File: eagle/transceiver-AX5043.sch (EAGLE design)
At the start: 43 parts, among them J1 142-0701-851, J2 142-0701-851, J3 142-0701-851, U1 U-ONSEMI-AX5043, U2 LP2985XX-N, X1 TAITIEN-TY

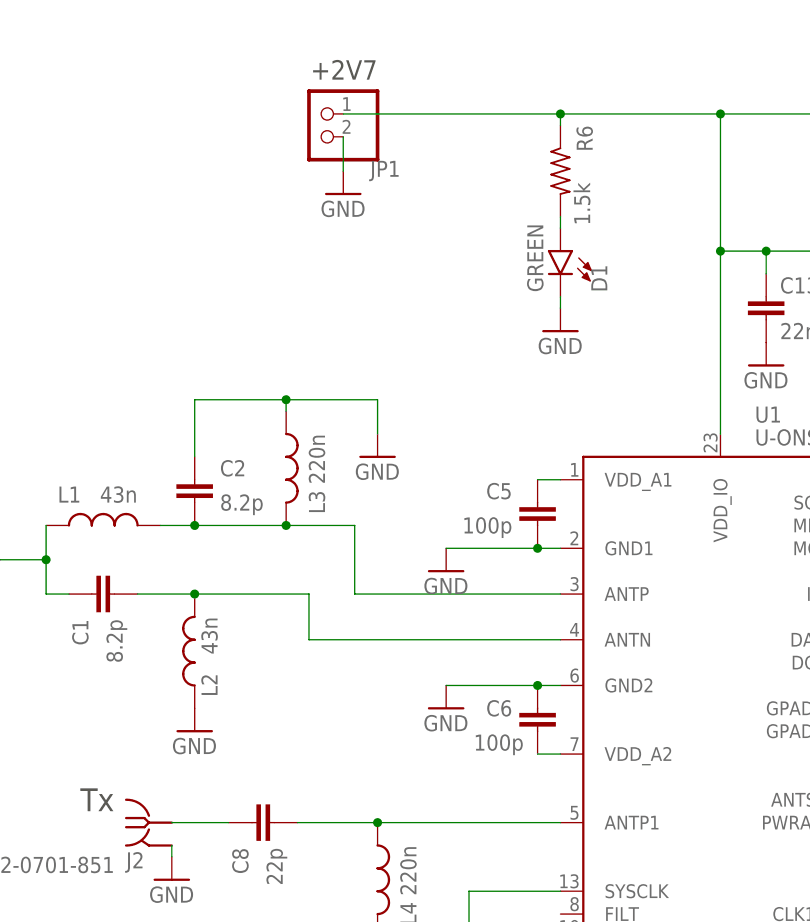
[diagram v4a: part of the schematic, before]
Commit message: Update AX5043
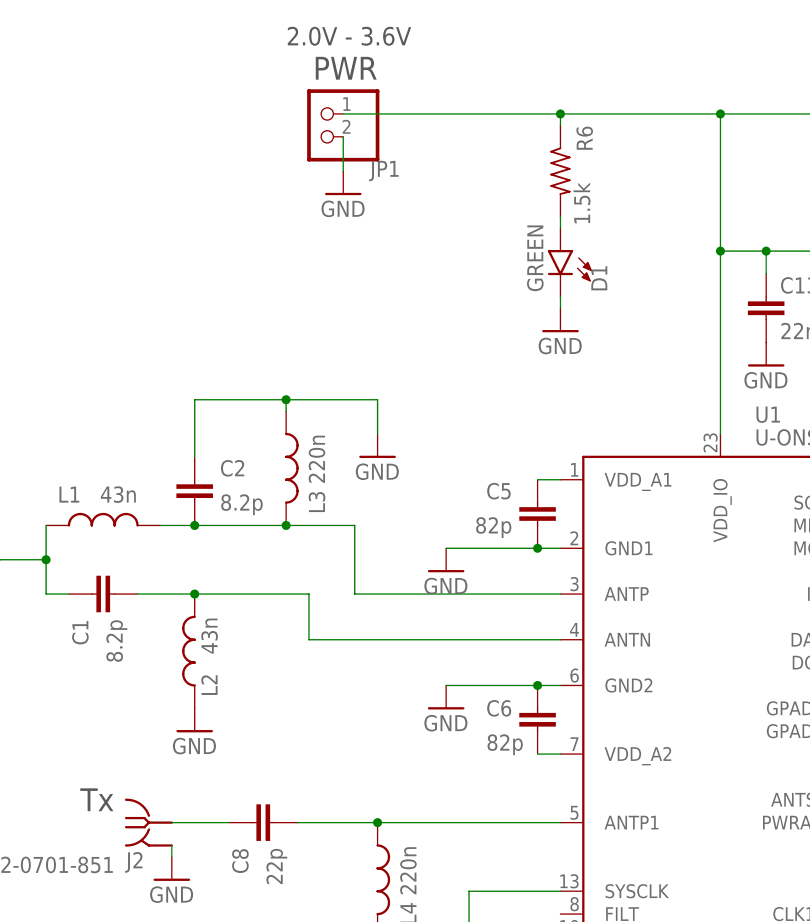
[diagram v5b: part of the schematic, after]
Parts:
- C5, C6: value 100p -> 82p
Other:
- note added: "2.0V - 3.6V"
- note added: "PWR"
- note removed: "+2V7"
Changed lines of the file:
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@@
 <?xml version="1.0" encoding="utf-8"?>
 <!DOCTYPE eagle SYSTEM "eagle.dtd">
-<eagle version="9.2.2">
+<eagle version="9.5.1">
 <drawing>
 <settings>
@@
 <part name="X1" library="X-Taitien-TY-TCXO" deviceset="TAITIEN-TY" device=""/>
 <part name="GND13" library="supply1" library_urn="urn:adsk.eagle:library:371" deviceset="GND" device=""/>
-<part name="C5" library="oresat-rcl" deviceset="C-EU" device="0402-C-NOSILK" value="100p"/>
-<part name="C6" library="oresat-rcl" deviceset="C-EU" device="0402-C-NOSILK" value="100p"/>
+<part name="C5" library="oresat-rcl" deviceset="C-EU" device="0402-C-NOSILK" value="82p"/>
+<part name="C6" library="oresat-rcl" deviceset="C-EU" device="0402-C-NOSILK" value="82p"/>
 <part name="L3" library="oresat-rcl" deviceset="L-US" device="0603-C-NOSILK" value="220n"/>
 <part name="L4" library="oresat-rcl" deviceset="L-US" device="0603-C-NOSILK" value="220n"/>
@@
 <text x="71.12" y="102.87" size="2.54" layer="97">Tx</text>
 <text x="59.69" y="77.47" size="2.54" layer="97">Ref-Out</text>
-<text x="104.14" y="184.15" size="2.159" layer="97" rot="MR0">+2V7</text>
+<text x="104.14" y="184.15" size="2.54" layer="97" rot="MR0">PWR</text>
 <text x="186.69" y="163.83" size="2.159" layer="97">SPI / IRQ</text>
 <text x="196.85" y="138.43" size="2.159" layer="97">Wire-Mode</text>
@@
 400 - 525 MHz
 800 - 1050 MHz</text>
+<text x="93.98" y="187.96" size="2.032" layer="97">2.0V - 3.6V</text>
 </plain>
 <instances>

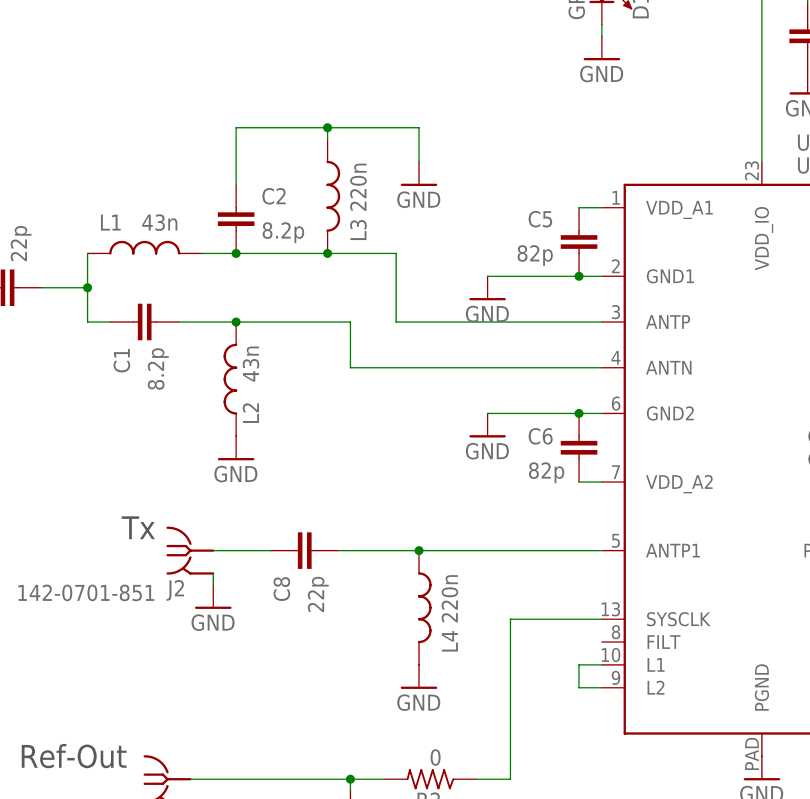
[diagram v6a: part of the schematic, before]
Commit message: Update AX5043 values
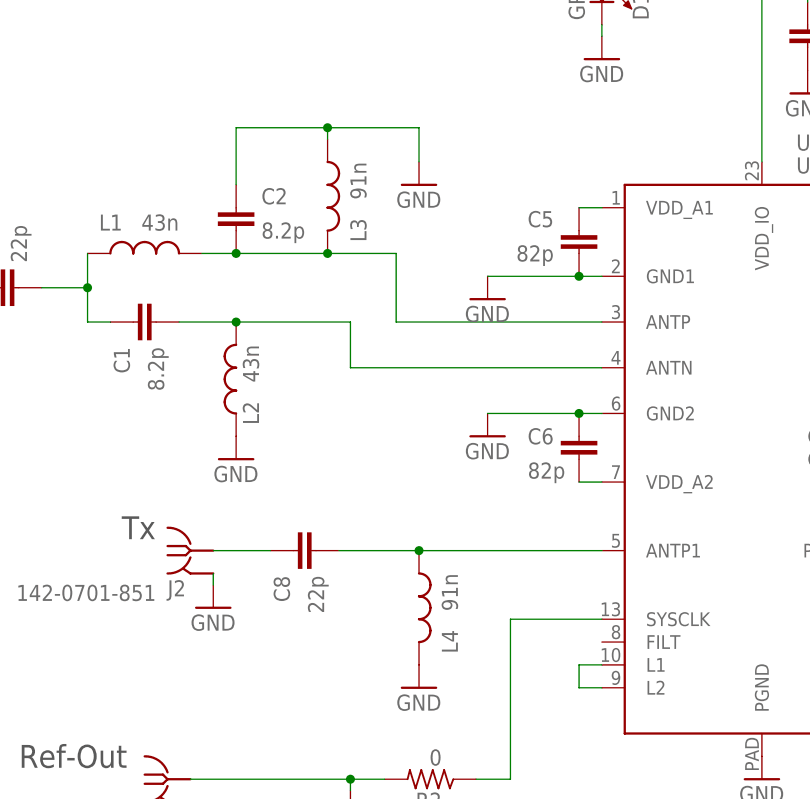
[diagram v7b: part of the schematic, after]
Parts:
- L3, L4: value 220n -> 91n
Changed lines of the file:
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@@
 <part name="C5" library="oresat-rcl" deviceset="C-EU" device="0402-C-NOSILK" value="82p"/>
 <part name="C6" library="oresat-rcl" deviceset="C-EU" device="0402-C-NOSILK" value="82p"/>
-<part name="L3" library="oresat-rcl" deviceset="L-US" device="0603-C-NOSILK" value="220n"/>
-<part name="L4" library="oresat-rcl" deviceset="L-US" device="0603-C-NOSILK" value="220n"/>
+<part name="L3" library="oresat-rcl" deviceset="L-US" device="0603-C-NOSILK" value="91n"/>
+<part name="L4" library="oresat-rcl" deviceset="L-US" device="0603-C-NOSILK" value="91n"/>
 <part name="C7" library="oresat-rcl" deviceset="C-EU" device="0402-C-NOSILK" value="22p"/>
 <part name="C8" library="oresat-rcl" deviceset="C-EU" device="0402-C-NOSILK" value="22p"/>

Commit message: Update values
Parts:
- R1: value 1k -> 150
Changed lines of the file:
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@@
 <part name="JP4" library="pinhead" library_urn="urn:adsk.eagle:library:325" deviceset="PINHD-1X6" device="" package3d_urn="urn:adsk.eagle:package:22472/2"/>
 <part name="GND11" library="supply1" library_urn="urn:adsk.eagle:library:371" deviceset="GND" device=""/>
-<part name="R1" library="oresat-rcl" deviceset="R-US_" device="0402-C-NOSILK" value="1k"/>
+<part name="R1" library="oresat-rcl" deviceset="R-US_" device="0402-C-NOSILK" value="150"/>
 <part name="C3" library="oresat-rcl" deviceset="C-EU" device="0402-C-NOSILK" value="1n"/>
 <part name="C4" library="oresat-rcl" deviceset="C-EU" device="0402-C-NOSILK" value="1n"/>
